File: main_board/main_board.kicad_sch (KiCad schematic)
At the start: 14 parts, among them SW1 SW_Push, SW2 SW_Push, U1 XIAO ESP32C3

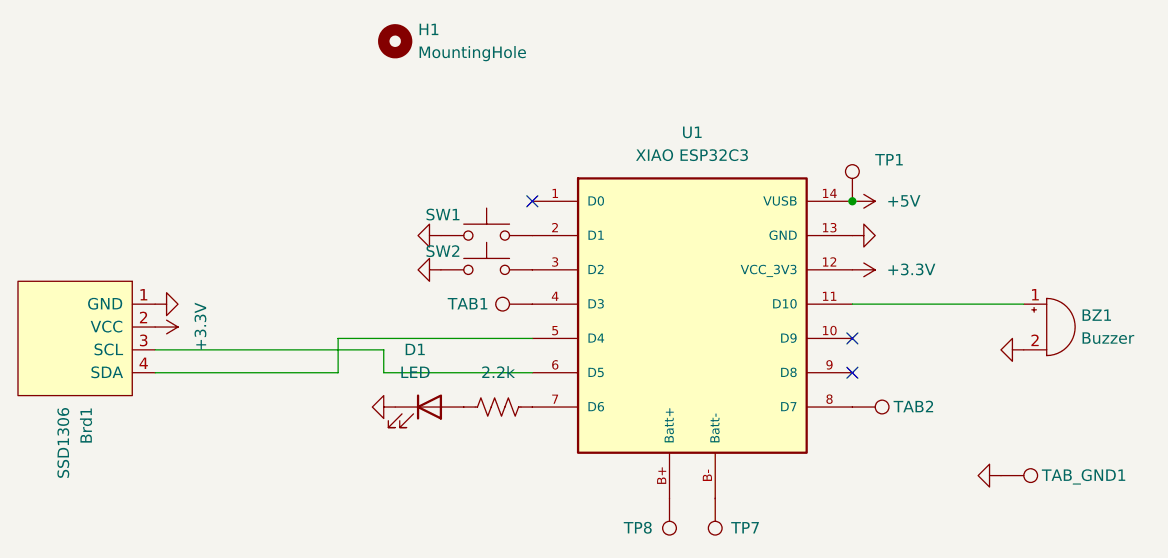
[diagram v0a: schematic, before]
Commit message: I updated the case in the hardware folder
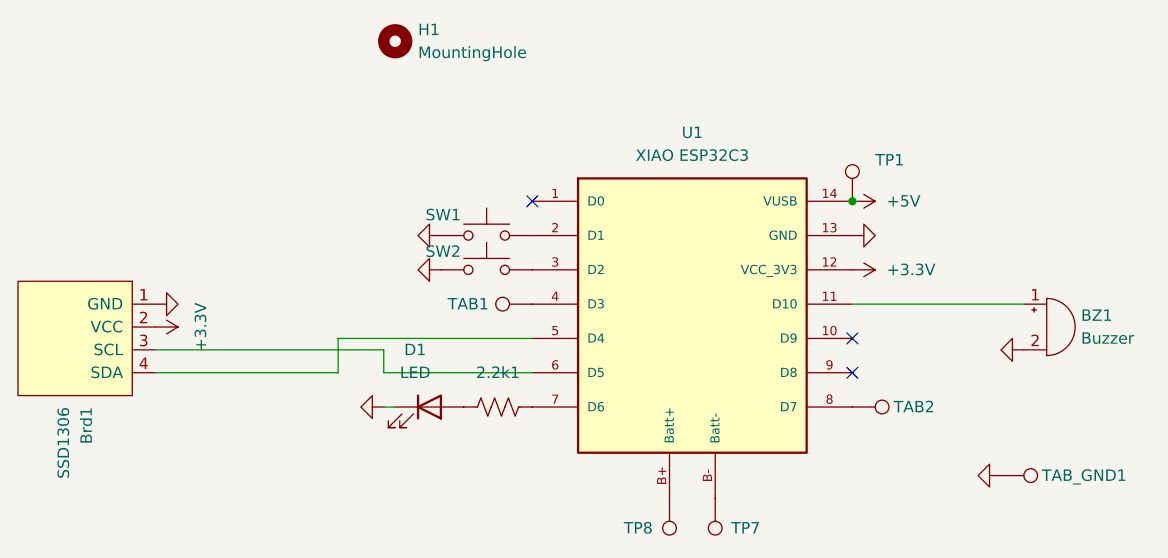
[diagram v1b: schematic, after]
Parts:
- renumbered 2.2k to 2.2k1
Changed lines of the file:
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@@
+		)
+	)
+	(wire
+		(pts
+			(xy 118.11 100.33) (xy 119.38 100.33)
+		)
+		(stroke
+			(width 0)
+			(type default)
 		)
 	)
@@
 		(dnp no)
 		(fields_autoplaced yes)
-		(property "Reference" "2.2k"
+		(property "Reference" "2.2k1"
 			(at 130.81 96.52 90)
 			(effects
@@
 			(project "main_board"
 				(path "/a93e7485-a3af-4678-b2d8-cd0dfdbad900"
-					(reference "2.2k")
+					(reference "2.2k1")
 					(unit 1)
 				)
@@
 	(symbol
 		(lib_id "power:GND")
-		(at 119.38 100.33 270)
+		(at 118.11 100.33 270)
 		(unit 1)
 		(exclude_from_sim no)
@@
 		(fields_autoplaced yes)
 		(property "Reference" "#PWR06"
-			(at 113.03 100.33 0)
+			(at 111.76 100.33 0)
 			(effects
 				(font
@@
 		)
 		(property "Value" "GND"
-			(at 115.57 100.3301 90)
+			(at 114.3 100.3301 90)
 			(effects
 				(font
@@
 		)
 		(property "Footprint" ""
-			(at 119.38 100.33 0)
+			(at 118.11 100.33 0)
 			(effects
 				(font
@@
 		)
 		(property "Datasheet" ""
-			(at 119.38 100.33 0)
+			(at 118.11 100.33 0)
 			(effects
 				(font
@@
 		)
 		(property "Description" "Power symbol creates a global label with name \"GND\" , ground"
-			(at 119.38 100.33 0)
-			(effects
-				(font
+			(at 118.11 100.33 0)
+			(effects
+				(font
